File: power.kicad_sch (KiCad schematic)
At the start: 28 parts, among them J1 USBC, Q2 BC817, SW3 SW_Push, U2 LM3670MF, U5 MCP73831-3-OT, U6 MAX17043G+T

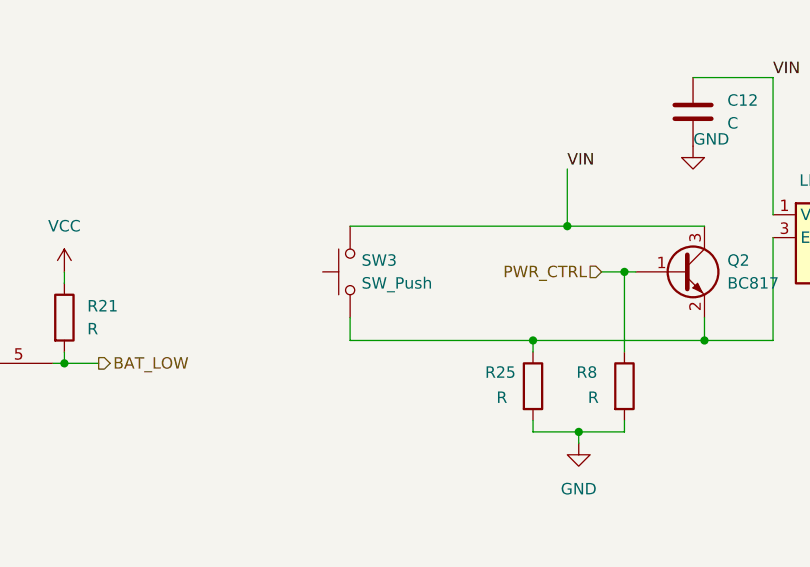
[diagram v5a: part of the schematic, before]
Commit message: Initial component placement
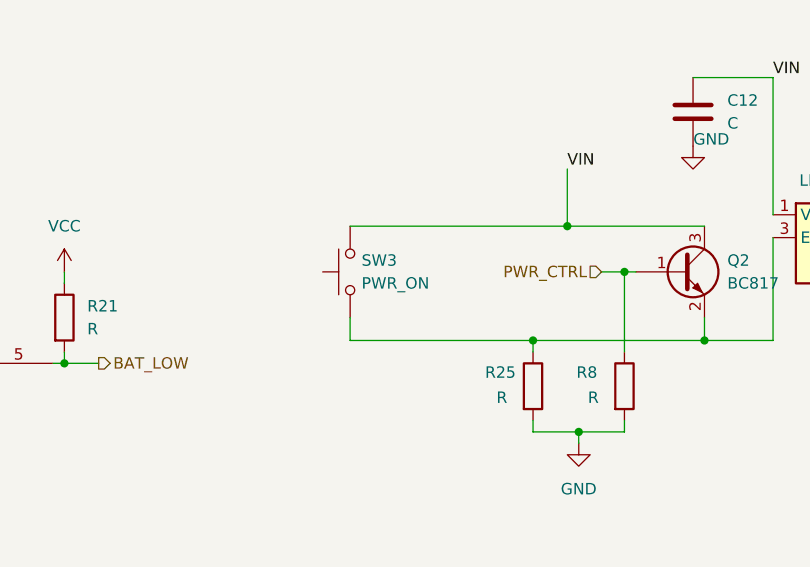
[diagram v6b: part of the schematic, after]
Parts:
- BT1: footprint (none) -> Battery:BatteryHolder_MPD_BH-18650-PC2
- C10, C11, C12, C16, C7, C8, C9: footprint (none) -> Capacitor_SMD:C_0805_2012Metric_Pad1.18x1.45mm_HandSolder
- D10, D11: footprint (none) -> Diode_SMD:D_0805_2012Metric_Pad1.15x1.40mm_HandSolder
- D12, D9: footprint (none) -> LED_SMD:LED_0805_2012Metric_Pad1.15x1.40mm_HandSolder
- J1: footprint (none) -> Connector_USB:USB_C_Receptacle_GCT_USB4125-xx-x_6P_TopMnt_Horizontal
- L1: footprint (none) -> Inductor_SMD_Wurth:L_Wurth_WE-LQSH-2010
- R18, R19, R20, R21, R22, R23, R24, R25, R8: footprint (none) -> Resistor_SMD:R_0805_2012Metric_Pad1.20x1.40mm_HandSolder
- SW3: value SW_Push -> PWR_ON; footprint (none) -> Button_Switch_SMD:SW_SPST_PTS647_Sx38
- U6: footprint 21-0174B_MXM -> Package_DFN_QFN:TDFN-8-1EP_3x2mm_P0.5mm_EP1.4x1.4mm
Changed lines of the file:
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@@
 			)
 		)
-		(property "Value" "SW_Push"
+		(property "Value" "PWR_ON"
 			(at 165.1 132.0799 90)
 			(effects
@@
 			)
 		)
-		(property "Footprint" ""
+		(property "Footprint" "Button_Switch_SMD:SW_SPST_PTS647_Sx38"
 			(at 158.75 130.81 0)
 			(effects
@@
 			)
 		)
-		(property "Footprint" ""
+		(property "Footprint" "Capacitor_SMD:C_0805_2012Metric_Pad1.18x1.45mm_HandSolder"
 			(at 213.0552 82.55 0)
 			(effects
@@
 			)
 		)
-		(property "Footprint" "21-0174B_MXM"
+		(property "Footprint" "Package_DFN_QFN:TDFN-8-1EP_3x2mm_P0.5mm_EP1.4x1.4mm"
 			(at 90.17 140.97 0)
 			(effects
@@
 			)
 		)
-		(property "Footprint" ""
+		(property "Footprint" "Resistor_SMD:R_0805_2012Metric_Pad1.20x1.40mm_HandSolder"
 			(at 73.152 71.12 90)
 			(effects
@@
 			)
 		)
-		(property "Footprint" ""
+		(property "Footprint" "Resistor_SMD:R_0805_2012Metric_Pad1.20x1.40mm_HandSolder"
 			(at 182.372 143.51 90)
 			(effects
@@
 			)
 		)
-		(property "Footprint" ""
+		(property "Footprint" "Resistor_SMD:R_0805_2012Metric_Pad1.20x1.40mm_HandSolder"
 			(at 74.93 128.778 90)
 			(effects
@@
 			)
 		)
-		(property "Footprint" ""
+		(property "Footprint" "LED_SMD:LED_0805_2012Metric_Pad1.15x1.40mm_HandSolder"
 			(at 252.73 128.27 0)
 			(effects
@@
 			)
 		)
-		(property "Footprint" ""
+		(property "Footprint" "Capacitor_SMD:C_0805_2012Metric_Pad1.18x1.45mm_HandSolder"
 			(at 83.5152 134.62 0)
 			(effects
@@
 			)
 		)
-		(property "Footprint" ""
+		(property "Footprint" "Capacitor_SMD:C_0805_2012Metric_Pad1.18x1.45mm_HandSolder"
 			(at 72.0852 168.91 0)
 			(effects
@@
 			)
 		)
-		(property "Footprint" ""
+		(property "Footprint" "Resistor_SMD:R_0805_2012Metric_Pad1.20x1.40mm_HandSolder"
 			(at 250.952 137.16 90)
 			(effects
@@
 			)
 		)
-		(property "Footprint" ""
+		(property "Footprint" "Resistor_SMD:R_0805_2012Metric_Pad1.20x1.40mm_HandSolder"
 			(at 130.302 135.89 90)
 			(effects
@@
 			)
 		)
-		(property "Footprint" ""
+		(property "Footprint" "Capacitor_SMD:C_0805_2012Metric_Pad1.18x1.45mm_HandSolder"
 			(at 242.2652 135.89 0)
 			(effects
@@
 			)
 		)
-		(property "Footprint" ""
+		(property "Footprint" "LED_SMD:LED_0805_2012Metric_Pad1.15x1.40mm_HandSolder"
 			(at 199.39 69.85 0)
 			(effects
@@
 			)
 		)
-		(property "Footprint" ""
+		(property "Footprint" "Capacitor_SMD:C_0805_2012Metric_Pad1.18x1.45mm_HandSolder"
 			(at 202.8952 116.84 0)
 			(effects
@@
 			)
 		)
-		(property "Footprint" ""
+		(property "Footprint" "Diode_SMD:D_0805_2012Metric_Pad1.15x1.40mm_HandSolder"
 			(at 173.99 69.85 0)
 			(effects
@@
 			)
 		)
-		(property "Footprint" ""
+		(property "Footprint" "Capacitor_SMD:C_0805_2012Metric_Pad1.18x1.45mm_HandSolder"
 			(at 82.2452 59.69 0)
 			(effects
@@
 			)
 		)
-		(property "Footprint" ""
+		(property "Footprint" "Capacitor_SMD:C_0805_2012Metric_Pad1.18x1.45mm_HandSolder"
 			(at 168.6052 81.28 0)
 			(effects
@@
 			)
 		)
-		(property "Footprint" ""
+		(property "Footprint" "Resistor_SMD:R_0805_2012Metric_Pad1.20x1.40mm_HandSolder"
 			(at 137.922 83.82 90)
 			(effects
@@
 			)
 		)
-		(property "Footprint" ""
+		(property "Footprint" "Inductor_SMD_Wurth:L_Wurth_WE-LQSH-2010"
 			(at 231.14 124.46 0)
 			(effects
@@
 			)
 		)
-		(property "Footprint" ""
+		(property "Footprint" "Resistor_SMD:R_0805_2012Metric_Pad1.20x1.40mm_HandSolder"
 			(at 197.612 81.28 90)
 			(effects
@@
 			)
 		)
-		(property "Footprint" ""
+		(property "Footprint" "Battery:BatteryHolder_MPD_BH-18650-PC2"
 			(at 177.8 77.216 90)
 			(effects
@@
 			)
 		)
-		(property "Footprint" ""
+		(property "Footprint" "Diode_SMD:D_0805_2012Metric_Pad1.15x1.40mm_HandSolder"
 			(at 163.83 66.04 0)
 			(effects
@@
 			)
 		)
-		(property "Footprint" ""
+		(property "Footprint" "Resistor_SMD:R_0805_2012Metric_Pad1.20x1.40mm_HandSolder"
 			(at 192.532 143.51 90)
 			(effects
@@
 			)
 		)
-		(property "Footprint" ""
+		(property "Footprint" "Connector_USB:USB_C_Receptacle_GCT_USB4125-xx-x_6P_TopMnt_Horizontal"
 			(at 53.34 55.88 0)
 			(effects
@@
 			)
 		)
-		(property "Footprint" ""
+		(property "Footprint" "Resistor_SMD:R_0805_2012Metric_Pad1.20x1.40mm_HandSolder"
 			(at 64.262 71.12 90)
 			(effects

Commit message: Initial layout
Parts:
- U6: footprint Package_DFN_QFN:TDFN-8-1EP_3x2mm_P0.5mm_EP1.4x1.4mm -> MAX17043:21-0174B_MXM
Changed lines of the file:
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@@
 	(label "SCL"
 		(at 66.04 146.05 0)
+		(fields_autoplaced yes)
 		(effects
 			(font
@@
 	(label "SDA"
 		(at 66.04 148.59 0)
+		(fields_autoplaced yes)
 		(effects
 			(font
@@
 			)
 		)
-		(property "Footprint" "Package_DFN_QFN:TDFN-8-1EP_3x2mm_P0.5mm_EP1.4x1.4mm"
+		(property "Footprint" "MAX17043:21-0174B_MXM"
 			(at 90.17 140.97 0)
 			(effects

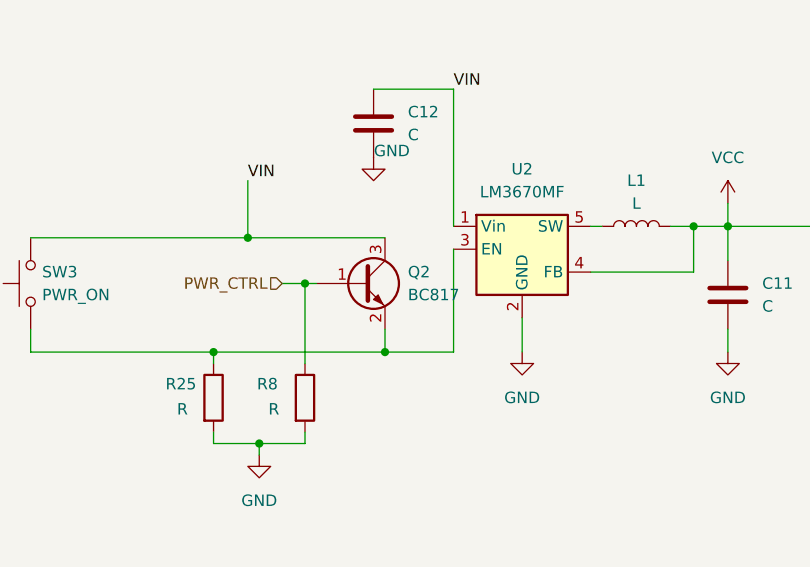
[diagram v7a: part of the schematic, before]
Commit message: Switch transistors to FETs
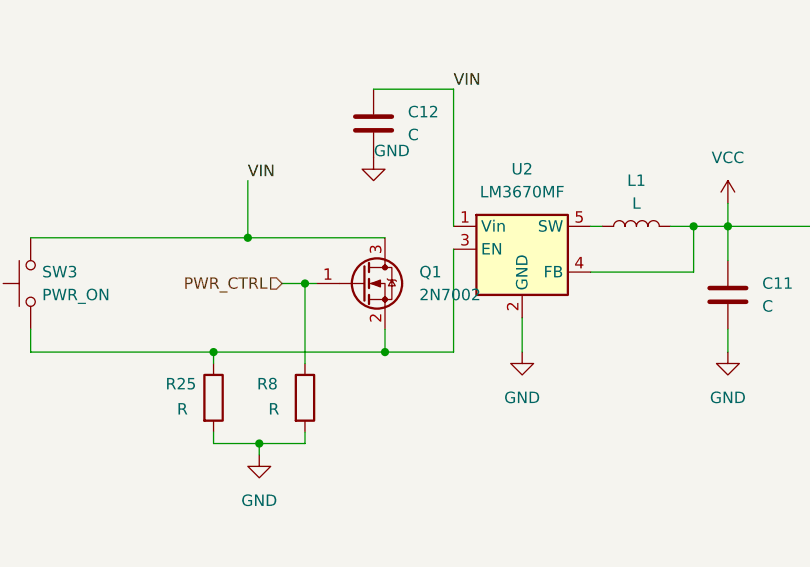
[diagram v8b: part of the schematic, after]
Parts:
- removed Q2: BC817, Package_TO_SOT_SMD:SOT-23, symbol Transistor_BJT:BC817
- added Q1: 2N7002, Package_TO_SOT_SMD:SOT-23, symbol Transistor_FET:2N7002
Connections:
- net PWR_CTRL: now also Q1.1 (G)
- net VIN: now also Q1.3 (D)
- net at R25.1, SW3.1, U2.3 (EN): now also Q1.2 (S)
